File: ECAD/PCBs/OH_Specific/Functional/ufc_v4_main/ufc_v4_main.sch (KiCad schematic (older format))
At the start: 18 parts, among them J1 PWR IN, P1 Digital, P2 Power, P3 Analog, P4 Analog, P5 PWM, P6 PWM, P7 Communication

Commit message: WIP Upload
Pausing work on main board to make some mods and finish up the AP, HUD, and UFC Mega Shield PCBs first. Will need to make some mods to the main board based on the outcome of those three PCBs.
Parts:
- removed J1: PWR IN, Connector_Molex:Molex_Micro-Fit_3.0_43045-0412_2x02_P3.00mm_Vertical, symbol Connector_Generic:Conn_02x02_Counter_Clockwise
- removed MK5, MK6: MH, Socket_Arduino_Mega:Arduino_1pin, symbol Mechanical:MountingHole
- removed P1: Digital, Connector_PinHeader_2.54mm:PinHeader_2x18_P2.54mm_Vertical, symbol Connector_Generic:Conn_02x18_Odd_Even
- removed P2: Power, Connector_PinHeader_2.54mm:PinHeader_1x08_P2.54mm_Vertical, symbol Connector_Generic:Conn_01x08
- removed P3, P4: Analog, Connector_PinHeader_2.54mm:PinHeader_1x08_P2.54mm_Vertical, symbol Connector_Generic:Conn_01x08
- removed P5: PWM, Connector_PinHeader_2.54mm:PinHeader_1x10_P2.54mm_Vertical, symbol Connector_Generic:Conn_01x10
- removed P6: PWM, Connector_PinHeader_2.54mm:PinHeader_1x08_P2.54mm_Vertical, symbol Connector_Generic:Conn_01x08
- removed P7: Communication, Connector_PinHeader_2.54mm:PinHeader_1x08_P2.54mm_Vertical, symbol Connector_Generic:Conn_01x08
- added C1, C11, C13, C15, C3, C5, C7, C9: 10uF, Capacitor_SMD:CP_Elec_4x5.3, symbol Device:CP_Small
- added C10, C12, C14, C16, C2, C4, C6, C8: 100nF, Capacitor_SMD:C_0402_1005Metric, symbol Device:C_Small
- added D1, D10, D11, D12, D13, D14, D15, D16, D17, D18, D19, D2, D20, D21, D22, D23, D24, D25, D26, D27, D28, D29, D3, D30, D31, D32, D33, D34, D35, D36, D4, D5, D6, D7, D8, D9: LED, LED_SMD:LED_0402_1005Metric, symbol Device:LED
- added J1: PWR IN, Connector_Molex:Molex_Mini-Fit_Jr_5566-08A2_2x04_P4.20mm_Vertical, symbol Connector_Generic:Conn_02x04_Top_Bottom
- added J10, J11, J12, J13, J14, J15, J16, J17, J18, J19, J2, J20, J21, J22, J23, J24, J25, J3, J31, J4, J5, J6, J7, J8, J9: Conn_01x05_Female, Connector_PinSocket_1.00mm:PinSocket_1x05_P1.00mm_Vertical, symbol Connector:Conn_01x05_Female
- added J26, J29: Conn_01x04_Female, Connector_PinSocket_1.00mm:PinSocket_1x04_P1.00mm_Vertical, symbol Connector:Conn_01x04_Female
- added J27: Conn_01x08_Female, Connector_PinSocket_1.00mm:PinSocket_1x08_P1.00mm_Vertical, symbol Connector:Conn_01x08_Female
- added J28, J30: Conn_01x07_Female, Connector_PinSocket_1.00mm:PinSocket_1x07_P1.00mm_Vertical, symbol Connector:Conn_01x07_Female
- added J32: HUD PANL, Connector_PinHeader_2.54mm:PinHeader_2x08_P2.54mm_Vertical_SMD, symbol Connector_Generic:Conn_02x08_Odd_Even
- added J33: PANEL SW, Connector_PinHeader_2.54mm:PinHeader_2x07_P2.54mm_Vertical_SMD, symbol Connector_Generic:Conn_02x07_Odd_Even
- added J34: AP BTNS, Connector_PinHeader_2.54mm:PinHeader_2x04_P2.54mm_Vertical_SMD, symbol Connector_Generic:Conn_02x04_Odd_Even
- added J35: HUD BIT, Connector_PinHeader_2.54mm:PinHeader_1x04_P2.54mm_Vertical_SMD_Pin1Left, symbol Connector:Conn_01x04_Male
- added P1: Conn_02x16_Odd_Even, Connector_PinHeader_2.54mm:PinHeader_2x16_P2.54mm_Vertical_SMD, symbol Connector_Generic:Conn_02x16_Odd_Even
- added P2: Conn_02x18_Odd_Even, Connector_PinHeader_2.54mm:PinHeader_2x18_P2.54mm_Vertical_SMD, symbol Connector_Generic:Conn_02x18_Odd_Even
- added R1, R13, R14, R2, R3, R7, R8, R9: 25.5K, Resistor_SMD:R_0603_1608Metric, symbol Device:R
- added R10, R11, R12, R15, R16, R4, R5, R6: 10K, Resistor_SMD:R_0603_1608Metric, symbol Device:R
- added SW1, SW10, SW11, SW12, SW13, SW14, SW15, SW16, SW17, SW18, SW19, SW2, SW3, SW4, SW5, SW6, SW7, SW8, SW9: TL1240GQ, KiCAD_Libraries:TL1240GQ, symbol KiCadCustomLib:TL1240GQ
- added U1, U2, U3, U4, U5, U6, U7, U8: MAX7219EWG+T, Package_SO:SOIC-24W_7.5x15.4mm_P1.27mm, symbol KiCadCustomLib:MAX7219EWG+T
- MK1, MK2, MK3, MK4: footprint Socket_Arduino_Mega:Arduino_1pin -> MountingHole:MountingHole_4.3mm_M4
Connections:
- net labels added: 0+, 0-, 1+, 1-, 2+, 2-, 3+, 3-, 4+, 4-, 5+, 5-, 6+, 6-, 7+, 7-, 8+, 8-, 9+, 9-, CLK, CLR+, CLR-, DIG0, DIG0_2, DIG0_3, DIG0_4, DIG0_5, DIG0_6, DIG0_7, DIG0_8, DIG1, DIG1_2, DIG1_3, DIG1_4, DIG1_5, DIG1_6, DIG1_7, DIG1_8, DIG2, DIG2_2, DIG2_3, DIG2_4, DIG2_5, DIG2_6, DIG2_7, DIG2_8, DIG3, DIG3_2, DIG3_3, DIG3_4, DIG3_5, DIG3_6, DIG3_7, DIG3_8, DIG4, DIG4_2, DIG4_3, DIG4_4, DIG4_5, DIG4_6, DIG4_7, DIG4_8, DIG5, DIG5_2, DIG5_3, DIG5_4, DIG5_5, DIG5_6, DIG5_7, DIG5_8, DIG6, DIG6_2, DIG6_3, DIG6_4, DIG6_5, DIG6_6, DIG6_7, DIG6_8, DIG7, DIG7_2, DIG7_3, DIG7_4, DIG7_5, DIG7_6, DIG7_7, DIG7_8, DIN2, DIN3, DIN4, DIN5, DIN6, DIN7, DIN8, DOT1+, DOT1+_2, DOT1+_3, DOT1+_4, DOT1+_5, DOT1-, DOT1-_2, DOT1-_3, DOT1-_4, DOT1-_5, DOT2+, DOT2+_2, DOT2+_3, DOT2+_4, DOT2+_5, DOT2-, DOT2-_2, DOT2-_3, DOT2-_4, DOT2-_5, EM+, EM-, ENT+, ENT-, IP+, IP-, LOAD(~CS), OP1+, OP1-, OP2+, OP2-, OP3+, OP3-, OP4+, OP4-, OP5+, OP5-, SEGA, SEGA_2, SEGA_3, SEGA_4, SEGA_5, SEGA_6, SEGA_7, SEGA_8, SEGB, SEGB_2, SEGB_3, SEGB_4, SEGB_5, SEGB_6, SEGB_7, SEGB_8, SEGC, SEGC_2, SEGC_3, SEGC_4, SEGC_5, SEGC_6, SEGC_7, SEGC_8, SEGD, SEGDP, SEGDP_2, SEGDP_3, SEGDP_4, SEGDP_5, SEGDP_6, SEGDP_7, SEGDP_8, SEGD_2, SEGD_3, SEGD_4, SEGD_5, SEGD_6, SEGD_7, SEGD_8, SEGE, SEGE_2, SEGE_3, SEGE_4, SEGE_5, SEGE_6, SEGE_7, SEGE_8, SEGF, SEGF_2, SEGF_3, SEGF_4, SEGF_5, SEGF_6, SEGF_7, SEGF_8, SEGG, SEGG_2, SEGG_3, SEGG_4, SEGG_5, SEGG_6, SEGG_7, SEGG_8
- net labels removed: +3.3V, +5VD, 0(Rx0), 1(Tx0), 14(Tx3), 15(Rx3), 16(Tx2), 17(Rx2), 18(Tx1), 19(Rx1), 20(SDA), 21(SCL), AREF, IOREF, Reset, SCL, SDA
- wire segments 97 -> 422
- no-connect marks 1 -> 13
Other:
- note added: "1)"
- note added: "ADF DWN"
- note added: "ADF UP"
- note added: "AP PANEL"
- note added: "BRT"
- note added: "BUS MASTER PWR\nSTD CONNECTOR"
- note added: "CLK & SCK\nMUST BE\nCONNECTED\nIN PARALLEL"
- note added: "COMM\n1 ENC"
- note added: "COMM\n2 ENC"
- note added: "COMM_1"
- note added: "COMM_2"
- note added: "HUD BIT TEST"
- note added: "HUD PANEL"
- note added: "ILLUMINATED TACT SWITCHES"
- note added: "OPT DISP LINE 1"
- note added: "OPT DISP LINE 2"
- note added: "OPT DISP LINE 3"
- note added: "OPT DISP LINE 4"
- note added: "OPT DISP LINE 5"
- note added: "OPT DOTS"
- note added: "OPT DOTS & COMM 1/2"
- note added: "OPT_DISP_1 CONN"
- note added: "OPT_DISP_2 CONN"
- note added: "OPT_DISP_3 CONN"
- note added: "OPT_DISP_4 CONN"
- note added: "OPT_DISP_5 CONN"
- note added: "PANEL MOUNTED \nUFC SWITCHES"
- note added: "PWR IN"
- note added: "SCRATCHPAD DIG 5-9"
- note added: "SCRATCHPAD DIG1-4 & OPT DOTS"
- note added: "SCRTPAD 16-SEG"
- note added: "SCRTPAD\nDIG #1 - #4"
- note added: "SCRTPAD\nDIG #5 - #9"
- note added: "U7 BACKLIGHT LEDS"
- note added: "U8 BACKLIGHT LEDS"
- note added: "VOL1"
- note added: "VOL2"
- note removed: "1"
- note removed: "1) XXXX"
- note removed: "NC"
- note removed: "NOTE: +5VD NET IS SAME \nAS +5V NET. IT IS BROKEN \nOUT TO SIMPLIFY ROUTING."
- note removed: "POWER IN"

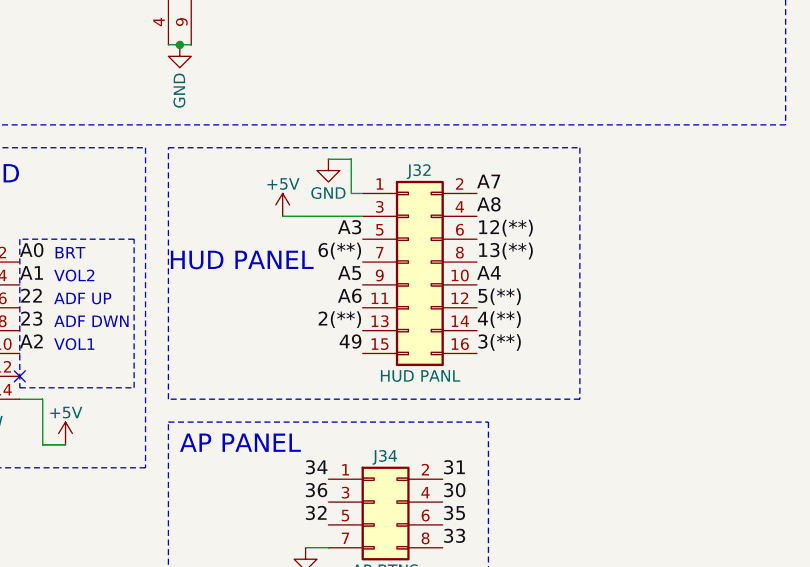
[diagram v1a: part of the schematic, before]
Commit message: UFC Display Milestone - Prototype Displays Ordered.
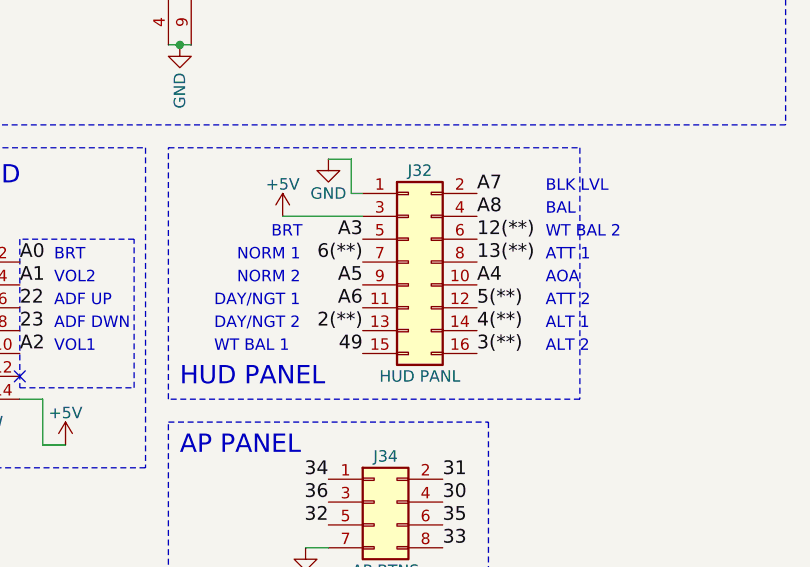
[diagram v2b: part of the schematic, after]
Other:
- note added: "ALT 1"
- note added: "ALT 2"
- note added: "AOA"
- note added: "ATT 1"
- note added: "ATT 2"
- note added: "BAL"
- note added: "BLK LVL"
- note added: "DAY/NGT 1"
- note added: "DAY/NGT 2"
- note added: "NORM 1"
- note added: "NORM 2"
- note added: "WT BAL 1"
- note added: "WT BAL 2"
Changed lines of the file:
@@
 EESchema Schematic File Version 4
 LIBS:ufc_v4_main-cache
-LIBS:ufc_v4_opt_daughterboard-cache
-LIBS:ufc_v4_opt-cache
-LIBS:ufc_v4_comm-cache
-LIBS:ufc_v4_scratchpad-cache
-LIBS:UFC_3.0-cache
-LIBS:ATX_PSU_Board-cache
-LIBS:ABSIS_Bus_Master-cache
 EELAYER 30 0
 EELAYER END
@@
 Text Label 17000 7350 0    60   ~ 0
 13(**)
-Text Notes 15650 7400 0    80   ~ 0
+Text Notes 15700 7900 0    80   ~ 0
 HUD PANEL
 $Comp
@@
 NoConn ~ 21050 1650
 NoConn ~ 21050 1750
+Text Notes 16100 7250 0    50   ~ 0
+BRT
+Text Notes 15950 7350 0    50   ~ 0
+NORM 1
+Text Notes 17300 7150 0    50   ~ 0
+BAL
+Text Notes 17300 7450 0    50   ~ 0
+AOA
+Text Notes 17300 7050 0    50   ~ 0
+BLK LVL
+Text Notes 15950 7450 0    50   ~ 0
+NORM 2
+Text Notes 15850 7550 0    50   ~ 0
+DAY/NGT 1
+Text Notes 15850 7650 0    50   ~ 0
+DAY/NGT 2
+Text Notes 15850 7750 0    50   ~ 0
+WT BAL 1
+Text Notes 17300 7250 0    50   ~ 0
+WT BAL 2
+Text Notes 17300 7350 0    50   ~ 0
+ATT 1
+Text Notes 17300 7550 0    50   ~ 0
+ATT 2
+Text Notes 17300 7650 0    50   ~ 0
+ALT 1
+Text Notes 17300 7750 0    50   ~ 0
+ALT 2
 $EndSCHEMATC

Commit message: Added UFC Controller PCB
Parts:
- removed J1: PWR IN, Connector_Molex:Molex_Mini-Fit_Jr_5566-08A2_2x04_P4.20mm_Vertical, symbol Connector_Generic:Conn_02x04_Top_Bottom
- removed J32: HUD PANL, Connector_PinHeader_2.54mm:PinHeader_2x08_P2.54mm_Vertical_SMD, symbol Connector_Generic:Conn_02x08_Odd_Even
- removed J33: PANEL SW, Connector_PinHeader_2.54mm:PinHeader_2x07_P2.54mm_Vertical_SMD, symbol Connector_Generic:Conn_02x07_Odd_Even
- removed J34: AP BTNS, Connector_PinHeader_2.54mm:PinHeader_2x04_P2.54mm_Vertical_SMD, symbol Connector_Generic:Conn_02x04_Odd_Even
- removed J35: HUD BIT, Connector_PinHeader_2.54mm:PinHeader_1x04_P2.54mm_Vertical_SMD_Pin1Left, symbol Connector:Conn_01x04_Male
- removed P1: Conn_02x16_Odd_Even, Connector_PinHeader_2.54mm:PinHeader_2x16_P2.54mm_Vertical_SMD, symbol Connector_Generic:Conn_02x16_Odd_Even
- removed P2: Conn_02x18_Odd_Even, Connector_PinHeader_2.54mm:PinHeader_2x18_P2.54mm_Vertical_SMD, symbol Connector_Generic:Conn_02x18_Odd_Even
- removed TP1: TP-12, TestPoint:TestPoint_THTPad_D1.5mm_Drill0.7mm, symbol Connector:TestPoint_Alt
- removed TP3: TP-3.3V, TestPoint:TestPoint_THTPad_D1.5mm_Drill0.7mm, symbol Connector:TestPoint_Alt
- added J0: PWR IN, Connector_Molex:Molex_Mini-Fit_Jr_5566-04A_2x02_P4.20mm_Vertical, symbol Connector_Generic:Conn_02x02_Odd_Even
- added J1: MAIN UFC I/O, symbol Connector_Generic:Conn_02x07_Odd_Even
- renumbered TP2 to TP1, TP4 to TP2
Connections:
- net 37 is gone; now on net 48: SW1.1, SW13.1, SW5.1, SW9.1
- net 39 is gone; now on net 44: SW11.1, SW15.1, SW3.1, SW7.1
- net +5V_SUPPLY: now also J0.1 (Pin_1), J0.2 (Pin_2)
- net 38: now also SW19.1, J1.14 (Pin_14); no longer SW10.1, SW14.1, SW2.1, SW6.1
- net 40: now also SW18.1, J1.12 (Pin_12); no longer SW12.1, SW16.1, SW17.1, SW4.1, SW8.1
- net 41: now also SW17.2, J1.13 (Pin_13); no longer SW1.2, SW2.2, SW3.2, SW4.2
- net 42: now also SW12.1, SW16.1, SW17.1, SW4.1, SW8.1, J1.10 (Pin_10); no longer SW5.2, SW6.2, SW7.2, SW8.2
- net 43: now also SW13.2, SW14.2, SW15.2, SW16.2, J1.11 (Pin_11); no longer SW10.2, SW11.2, SW12.2, SW9.2
- net 44: now also J1.8 (Pin_8); no longer SW13.2, SW14.2, SW15.2, SW16.2
- net 45: now also SW10.2, SW11.2, SW12.2, SW9.2, J1.9 (Pin_9); no longer SW17.2
- net 46: now also SW10.1, SW14.1, SW2.1, SW6.1, J1.6 (Pin_6); no longer SW18.1
- net 47: now also SW5.2, SW6.2, SW7.2, SW8.2, J1.7 (Pin_7); no longer SW19.1
- net 48: now also J1.4 (Pin_4)
- net 49: now also SW1.2, SW2.2, SW3.2, SW4.2, J1.5 (Pin_5)
- net 52(SCK): now also J1.2 (Pin_2)
- net 53(SS): now also J1.1 (Pin_1)
- net GND: now also J0.3 (Pin_3), J0.4 (Pin_4)
- net 51(MOSI) renamed DIN
- net DIN: now also J1.3 (Pin_3)
- no-connect marks 13 -> 1
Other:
- note added: "1) XXXX"
- note added: "CONNECTORS"
- note added: "EMCON SW"
- note added: "I/P SW"
- note added: "KEY MTX COL 1"
- note added: "KEY MTX COL 2"
- note added: "KEY MTX COL 3"
- note added: "KEY MTX COL 4"
- note added: "KEY MTX ROW 1"
- note added: "KEY MTX ROW 2"
- note added: "KEY MTX ROW 3"
- note added: "KEY MTX ROW 4"
- note added: "KEY MTX ROW 5"
- note removed: "1)"
- note removed: "ADF DWN"
- note removed: "ADF UP"
- note removed: "ALT 1"
- note removed: "ALT 2"
- note removed: "AOA"
- note removed: "AP PANEL"
- note removed: "ARDUINO MEGA REV3"
- note removed: "ATT 1"
- note removed: "ATT 2"
- note removed: "BAL"
- note removed: "BLK LVL"
- note removed: "BRT"
- note removed: "BUS MASTER PWR\nSTD CONNECTOR"
- note removed: "COMM\n1 ENC"
- note removed: "COMM\n2 ENC"
- note removed: "DAY/NGT 1"
- note removed: "DAY/NGT 2"
- note removed: "HUD BIT TEST"
- note removed: "HUD PANEL"
- note removed: "NORM 1"
- note removed: "NORM 2"
- note removed: "PANEL MOUNTED \nUFC SWITCHES"
- note removed: "PWR IN"
- note removed: "VOL1"
- note removed: "VOL2"
- note removed: "WT BAL 1"
- note removed: "WT BAL 2"
- moved on the sheet: C1, C10, C11, C12, C13, C14, C15, C16, C2, C3, C4, C5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

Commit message: UFC WIP
Adding AP PCB, UFC Main PCB. PCBs should be complete.
MCAD: AP Module Complete, starting UFC MCAD update in earnest.
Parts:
- J1: footprint (none) -> Connector_PinHeader_2.54mm:PinHeader_2x07_P2.54mm_Vertical
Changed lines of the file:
@@
 F 0 "J1" H 20150 1817 50  0000 C CNN
 F 1 "MAIN UFC I/O" H 20150 1726 50  0000 C CNN
-F 2 "" H 20100 1300 50  0001 C CNN
+F 2 "Connector_PinHeader_2.54mm:PinHeader_2x07_P2.54mm_Vertical" H 20100 1300 50  0001 C CNN
 F 3 "~" H 20100 1300 50  0001 C CNN
 	1    20100 1300

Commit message: Update main UFC board, to send all segment signals to SCRATCHPAD, COMM1 and COMM2. this will make the software simpler Update main UFC board, POT mounting holes are now first class citizens. Update main UFC board, most layers are filled with ground. in2 is power. Fix main UFC board having isolated grounds. Corrected LED on the 16 segment display binary representation  in UFCconnections.xlsx
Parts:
- added MK5: SW_ADF, MountingHole:MountingHole_6.4mm_M6, symbol Mechanical:MountingHole
- added POT1: VOL1, OHSwitches:BR10K_Pot_11mm_x_11mm, symbol Mechanical:MountingHole
- added POT2: VOL2, OHSwitches:BR10K_Pot_11mm_x_11mm, symbol Mechanical:MountingHole
- added POT3: BRT, OHSwitches:BR10K_Pot_11mm_x_11mm, symbol Mechanical:MountingHole
- SW1, SW10, SW11, SW12, SW13, SW14, SW15, SW16, SW17, SW18, SW19, SW2, SW3, SW4, SW5, SW6, SW7, SW8, SW9: symbol KiCadCustomLib:TL1240GQ -> ufc_v4_main-rescue:TL1240GQ-KiCadCustomLib
- U1, U2, U3, U4, U5, U6, U7, U8: symbol KiCadCustomLib:MAX7219EWG+T -> ufc_v4_main-rescue:MAX7219EWG+T-KiCadCustomLib
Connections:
- net DIG0_6: now also J14.1 (Pin_1); no longer J14.3 (Pin_3), J20.3 (Pin_3), J27.1 (Pin_1)
- net DIG1_6: now also J14.2 (Pin_2); no longer J14.4 (Pin_4), J20.4 (Pin_4), J27.2 (Pin_2)
- net DIG2_6: now also J20.1 (Pin_1); no longer J14.5 (Pin_5), J20.5 (Pin_5), J27.3 (Pin_3)
- net DIG3_6: now also J20.2 (Pin_2); no longer J15.1 (Pin_1), J21.1 (Pin_1), J27.4 (Pin_4)
- net DIG4_6: now also J26.1 (Pin_1); no longer J15.2 (Pin_2), J21.2 (Pin_2), J27.5 (Pin_5)
- net DIG5_6: now also J26.2 (Pin_2); no longer J15.3 (Pin_3), J21.3 (Pin_3), J27.6 (Pin_6)
- net DIG6_6: now also J26.3 (Pin_3); no longer J15.4 (Pin_4), J21.4 (Pin_4), J27.7 (Pin_7)
- net DIG7_6: now also J26.4 (Pin_4); no longer J15.5 (Pin_5), J21.5 (Pin_5), J27.8 (Pin_8)
- net SEGA_6: now also J14.4 (Pin_4), J20.4 (Pin_4), J27.2 (Pin_2); no longer J14.2 (Pin_2)
- net SEGB_6: now also J14.5 (Pin_5), J20.5 (Pin_5), J27.3 (Pin_3); no longer J20.1 (Pin_1)
- net SEGC_6: now also J15.1 (Pin_1), J21.1 (Pin_1), J27.4 (Pin_4); no longer J20.2 (Pin_2)
- net SEGDP_6: now also J14.3 (Pin_3), J20.3 (Pin_3), J27.1 (Pin_1); no longer J14.1 (Pin_1)
- net SEGD_6: now also J15.2 (Pin_2), J21.2 (Pin_2), J27.5 (Pin_5); no longer J26.1 (Pin_1)
- net SEGE_6: now also J15.3 (Pin_3), J21.3 (Pin_3), J27.6 (Pin_6); no longer J26.2 (Pin_2)
- net SEGF_6: now also J15.4 (Pin_4), J21.4 (Pin_4), J27.7 (Pin_7); no longer J26.3 (Pin_3)
- net SEGG_6: now also J15.5 (Pin_5), J21.5 (Pin_5), J27.8 (Pin_8); no longer J26.4 (Pin_4)
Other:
- note added: "COMM 1/2 & scratch 16seg"
- note added: "Potentiometer and ADF switch mounting holes"
- note removed: "OPT DOTS & COMM 1/2"
- moved on the sheet: J20, J21, J26, J27

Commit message: Revert "Merge branch 'ABSIS_2.0' of https://github.com/jrsteensen/OpenHornet into ABSIS_2.0"
This reverts commit cac173c4110ad9f0d1ad5a88a6b4048d6b756427, reversing
changes made to d0a675c2168bb1c3cb62f6e4a84cc7e34bb45d3d.
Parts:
- removed MK5: SW_ADF, MountingHole:MountingHole_6.4mm_M6, symbol Mechanical:MountingHole
- removed POT1: VOL1, OHSwitches:BR10K_Pot_11mm_x_11mm, symbol Mechanical:MountingHole
- removed POT2: VOL2, OHSwitches:BR10K_Pot_11mm_x_11mm, symbol Mechanical:MountingHole
- removed POT3: BRT, OHSwitches:BR10K_Pot_11mm_x_11mm, symbol Mechanical:MountingHole
- SW1, SW10, SW11, SW12, SW13, SW14, SW15, SW16, SW17, SW18, SW19, SW2, SW3, SW4, SW5, SW6, SW7, SW8, SW9: symbol ufc_v4_main-rescue:TL1240GQ-KiCadCustomLib -> KiCadCustomLib:TL1240GQ
- U1, U2, U3, U4, U5, U6, U7, U8: symbol ufc_v4_main-rescue:MAX7219EWG+T-KiCadCustomLib -> KiCadCustomLib:MAX7219EWG+T
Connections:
- net DIG0_6: now also J14.3 (Pin_3), J20.3 (Pin_3), J27.1 (Pin_1); no longer J14.1 (Pin_1)
- net DIG1_6: now also J14.4 (Pin_4), J20.4 (Pin_4), J27.2 (Pin_2); no longer J14.2 (Pin_2)
- net DIG2_6: now also J14.5 (Pin_5), J20.5 (Pin_5), J27.3 (Pin_3); no longer J20.1 (Pin_1)
- net DIG3_6: now also J15.1 (Pin_1), J21.1 (Pin_1), J27.4 (Pin_4); no longer J20.2 (Pin_2)
- net DIG4_6: now also J15.2 (Pin_2), J21.2 (Pin_2), J27.5 (Pin_5); no longer J26.1 (Pin_1)
- net DIG5_6: now also J15.3 (Pin_3), J21.3 (Pin_3), J27.6 (Pin_6); no longer J26.2 (Pin_2)
- net DIG6_6: now also J15.4 (Pin_4), J21.4 (Pin_4), J27.7 (Pin_7); no longer J26.3 (Pin_3)
- net DIG7_6: now also J15.5 (Pin_5), J21.5 (Pin_5), J27.8 (Pin_8); no longer J26.4 (Pin_4)
- net SEGA_6: now also J14.2 (Pin_2); no longer J14.4 (Pin_4), J20.4 (Pin_4), J27.2 (Pin_2)
- net SEGB_6: now also J20.1 (Pin_1); no longer J14.5 (Pin_5), J20.5 (Pin_5), J27.3 (Pin_3)
- net SEGC_6: now also J20.2 (Pin_2); no longer J15.1 (Pin_1), J21.1 (Pin_1), J27.4 (Pin_4)
- net SEGDP_6: now also J14.1 (Pin_1); no longer J14.3 (Pin_3), J20.3 (Pin_3), J27.1 (Pin_1)
- net SEGD_6: now also J26.1 (Pin_1); no longer J15.2 (Pin_2), J21.2 (Pin_2), J27.5 (Pin_5)
- net SEGE_6: now also J26.2 (Pin_2); no longer J15.3 (Pin_3), J21.3 (Pin_3), J27.6 (Pin_6)
- net SEGF_6: now also J26.3 (Pin_3); no longer J15.4 (Pin_4), J21.4 (Pin_4), J27.7 (Pin_7)
- net SEGG_6: now also J26.4 (Pin_4); no longer J15.5 (Pin_5), J21.5 (Pin_5), J27.8 (Pin_8)
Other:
- note added: "OPT DOTS & COMM 1/2"
- note removed: "COMM 1/2 & scratch 16seg"
- note removed: "Potentiometer and ADF switch mounting holes"
- moved on the sheet: J20, J21, J26, J27
